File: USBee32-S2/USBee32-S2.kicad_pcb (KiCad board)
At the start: 4 copper layers, 28.1 x 68.3 mm, 52 parts, among them J1 USB_A, J2 TYPE-C-31-M-12, J3 Conn_01x18_Male, J4 B2B-PH-SM4-TB(LF)(SN), J5 Conn_01x22_Male, Q1 MMBT8050, Q2 MMBT8050, SW1 SW_Push, SW2 SW_Push, U1 ESP32-S2-WROOM-ESP32-S2-WROOM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

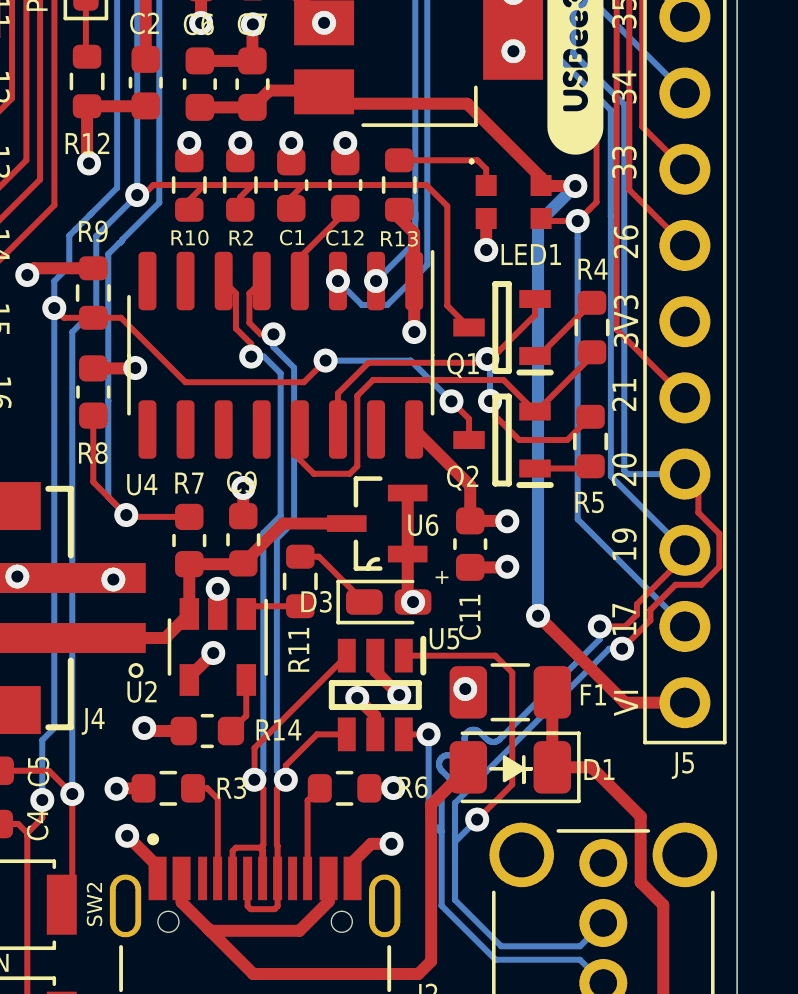
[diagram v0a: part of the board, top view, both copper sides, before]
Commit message: Fixed Battery Charging Circuit
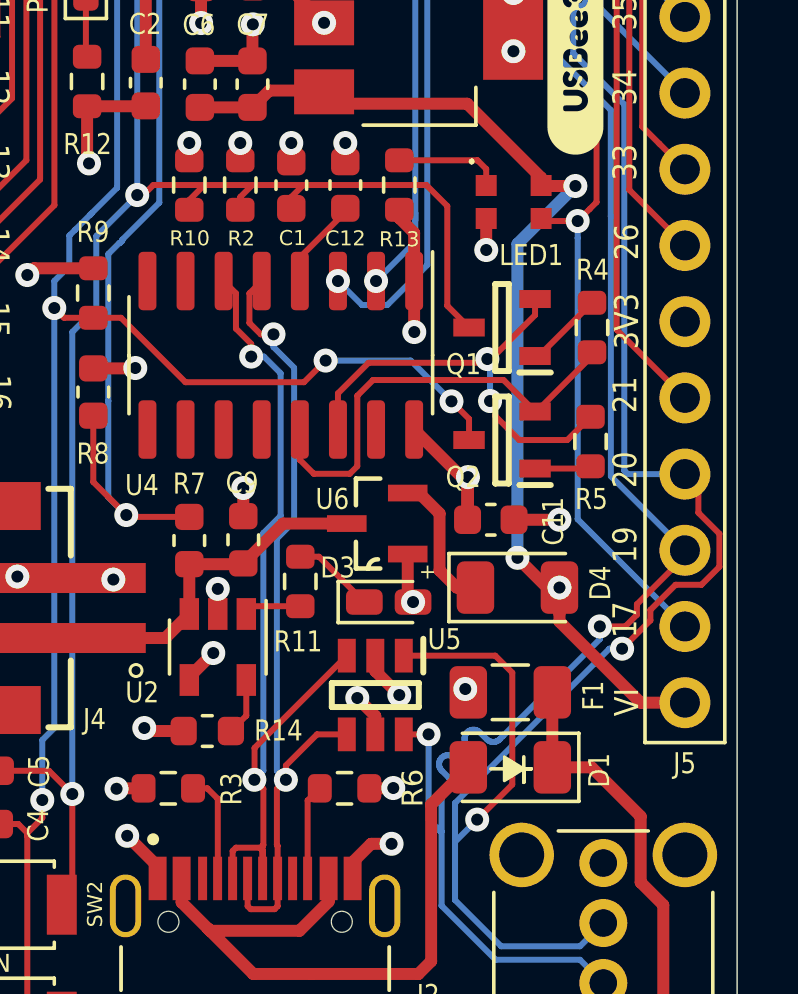
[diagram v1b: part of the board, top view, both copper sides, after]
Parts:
- added D4: 1N5819, Diode_SMD:D_1206_3216Metric, F.Cu at (186.6, 107.5)
- moved C11 1.06 mm to (185.8, 105.3), turned to 0 degrees
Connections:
- U6 pad 2: /VI -> Net-(D4-Pad1)
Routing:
- net Net-(D4-Pad1): track 0.00 -> 4.67 mm
- net /VI: track 42.1 -> 40.6 mm, vias 6 -> 7
